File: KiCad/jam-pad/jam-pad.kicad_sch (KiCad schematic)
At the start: 63 parts, among them J1 USB_C, J2 PH_01x03_2.54mm, SW1 MX_Hotswap_LED_RGB, SW13 SW_Push, SW14 RotaryEncoder_Switch, SW15 SW_Push, SW2 MX_Hotswap_LED_RGB, SW3 MX_Hotswap_LED_RGB, SW4 MX_Hotswap_LED_RGB, SW5 MX_Hotswap_LED_RGB, SW6 MX_Hotswap_LED_RGB, SW7 MX_Hotswap_LED_RGB, SW8 MX_Hotswap_LED_RGB, SW9 MX_Hotswap_LED_RGB, U1 RP2040, U3 W25Q16JVSNIQ, U4 MIC5319-3.3YD5, Y1 ECS-120-18-33-JGN

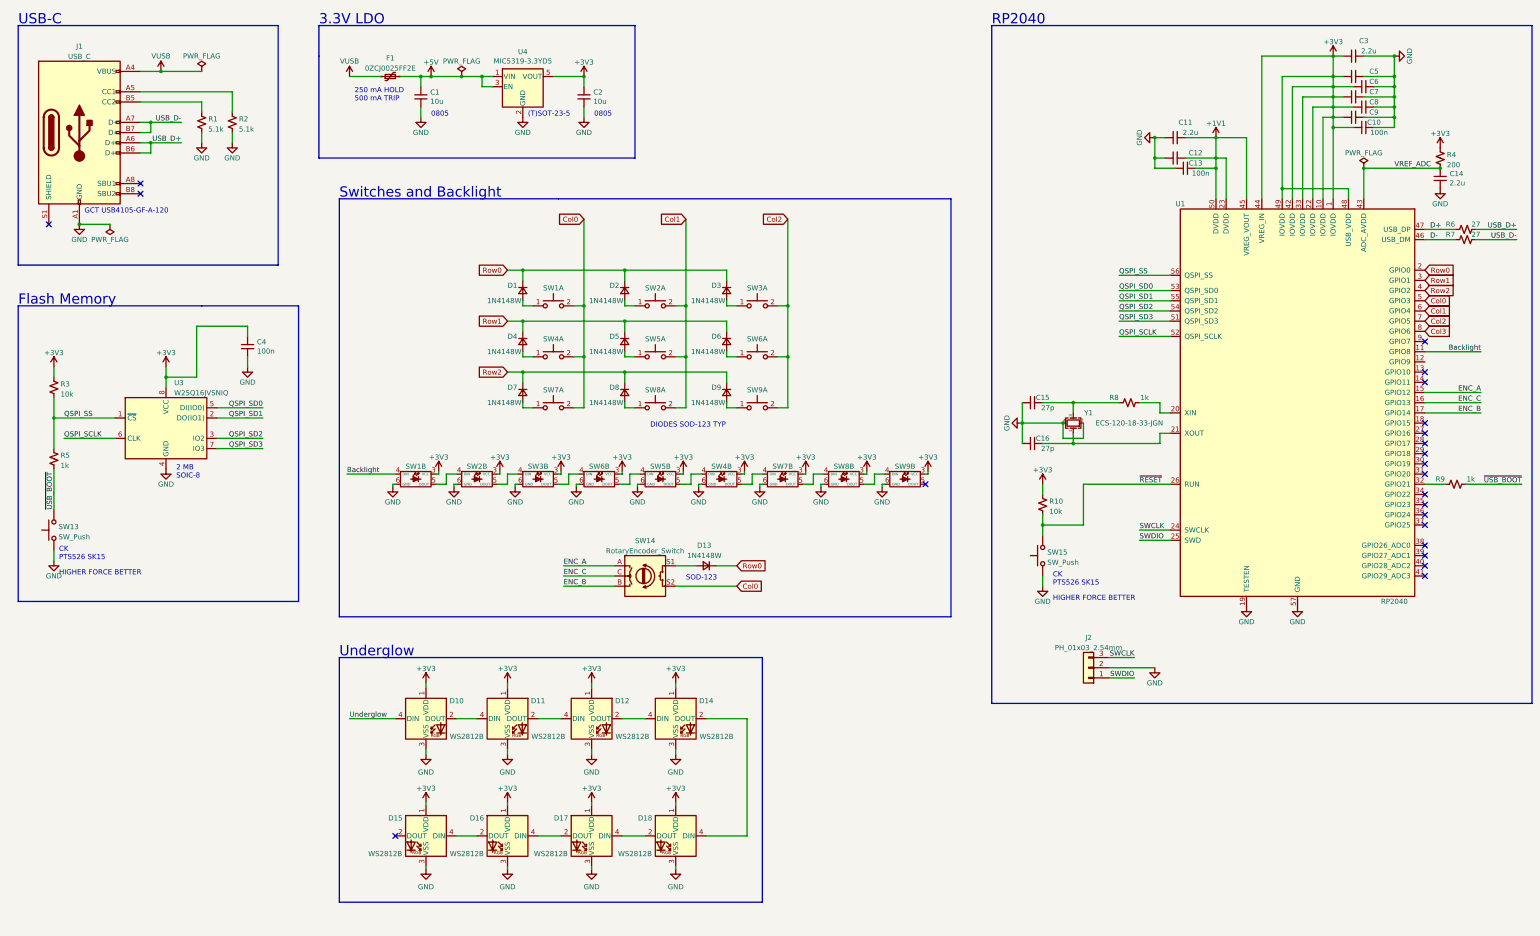
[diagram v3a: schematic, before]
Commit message: changed underglow to knoblight, added led c and r, placed leds
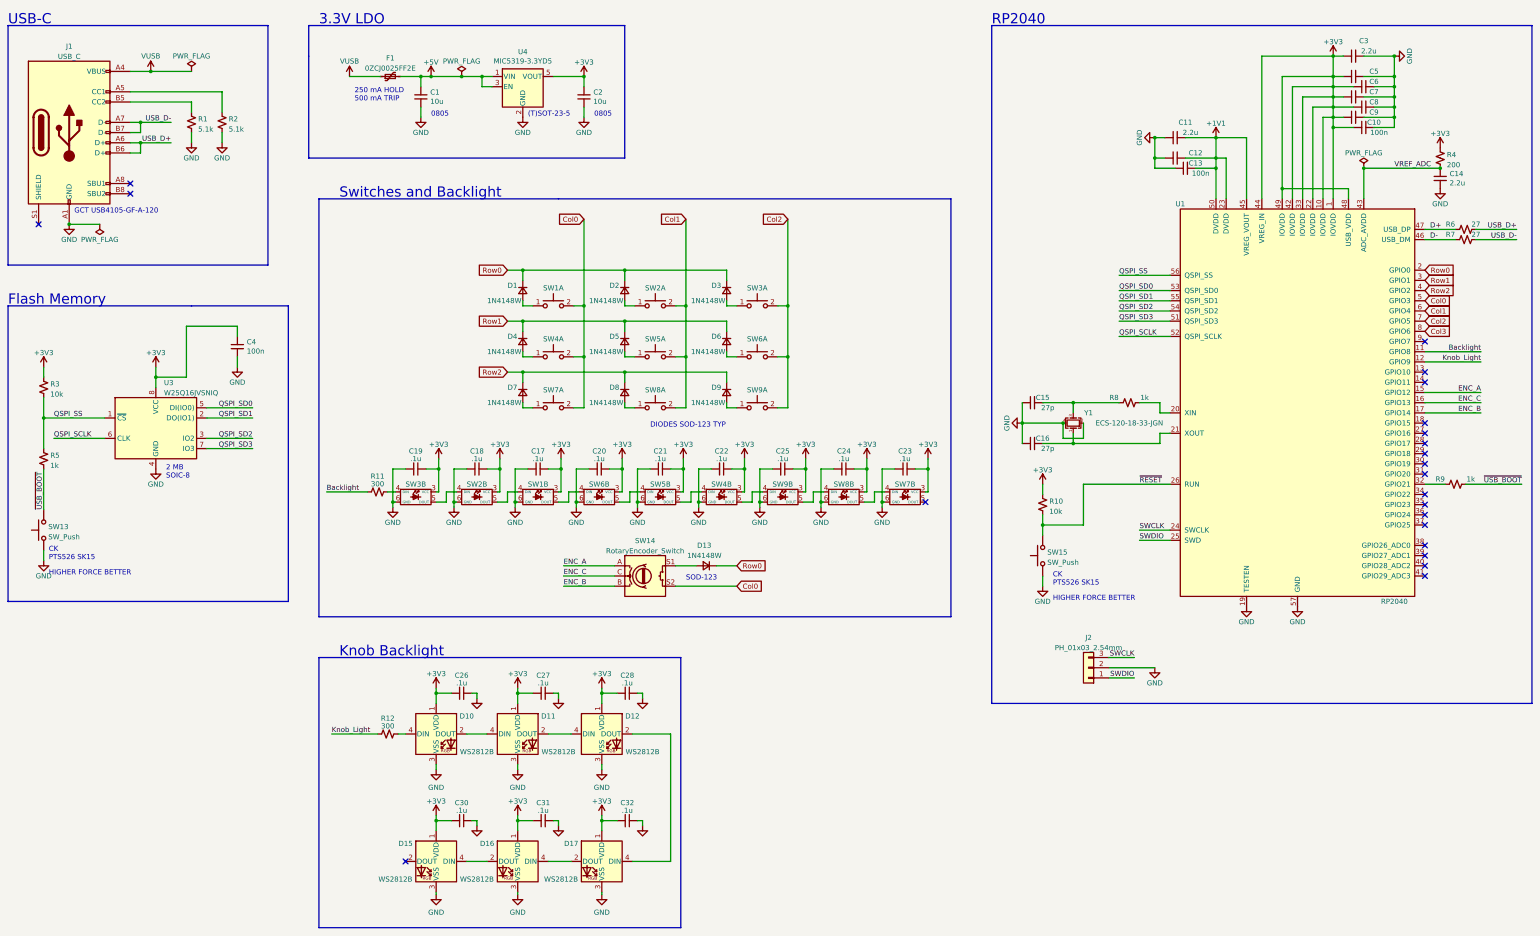
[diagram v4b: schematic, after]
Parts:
- removed D14, D18: WS2812B, LED_SMD:LED_WS2812B_PLCC4_5.0x5.0mm_P3.2mm, symbol LED:WS2812B
- added C17, C18, C19, C20, C21, C22, C23, C24, C25, C26, C27, C28, C30, C31, C32: .1u, Capacitor_SMD:C_0603_1608Metric_Pad1.08x0.95mm_HandSolder, symbol Device:C_Small
- added R11, R12: 300, Resistor_SMD:R_0603_1608Metric_Pad0.98x0.95mm_HandSolder, symbol Device:R_Small_US
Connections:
- net +3V3: now also C17.1, C18.1, C19.1, C20.1, C21.1, C22.1, C23.1, C24.1, C25.1, C26.2, C27.2, C28.2, C30.2, C31.2, C32.2
- net Backlight: now also R11.1; no longer SW1.4 (DIN)
- net GND: now also C17.2, C18.2, C19.2, C20.2, C21.2, C22.2, C23.2, C24.2, C25.2, C26.1, C27.1, C28.1, C30.1, C31.1, C32.1
- net at D17.4 (DIN): now also D12.2 (DOUT)
- net at SW9.4 (DIN): now also SW4.5 (DOUT); no longer SW8.5 (DOUT)
- net at SW9.5 (DOUT): now also SW8.4 (DIN)
- net Knob_Light: now reaches U1.12 (GPIO9)
- net Knob_Light: now also R12.1
- net at SW6.4 (DIN): now also SW1.5 (DOUT); no longer SW3.5 (DOUT)
- net at SW2.4 (DIN): now also SW3.5 (DOUT); no longer SW1.5 (DOUT)
- net at SW3.4 (DIN): now also R11.2; no longer SW2.5 (DOUT)
- net at SW7.5 (DOUT): no longer SW8.4 (DIN)
- net at SW7.4 (DIN): now also SW8.5 (DOUT); no longer SW4.5 (DOUT)
- net Underglow: no longer names the net of D10.4 (DIN)
- net Underglow: now also R12.2
- new net: SW1.4 (DIN), SW2.5 (DOUT)
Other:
- note added: "Knob Backlight"
- note removed: "Underglow"
- moved on the sheet: C4, D10, D11, D12, D15, D16, D17, J1, R1, R2, R3, R5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

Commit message: initial routing
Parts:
- SW1, SW2, SW3, SW7, SW8, SW9: footprint jam-pad:MXOnly-1U-Hotswap-SK6812MINI-E -> jam-pad:MXOnly-1U-Hotswap-SK6812MINI-E_180
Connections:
- net at R11.2: now also SW1.4 (DIN); no longer SW3.4 (DIN)
- net at SW9.4 (DIN): now also SW8.5 (DOUT); no longer SW4.5 (DOUT)
- net at SW9.5 (DOUT): no longer SW8.4 (DIN)
- net at SW6.4 (DIN): now also SW3.5 (DOUT); no longer SW1.5 (DOUT)
- net at SW2.5 (DOUT): now also SW3.4 (DIN); no longer SW1.4 (DIN)
- net at SW2.4 (DIN): now also SW1.5 (DOUT); no longer SW3.5 (DOUT)
- net at SW7.4 (DIN): now also SW4.5 (DOUT); no longer SW8.5 (DOUT)
- net at SW7.5 (DOUT): now also SW8.4 (DIN)
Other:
- moved on the sheet: C17, C19, C23, C25, SW1B, SW3B, SW7B, SW9B

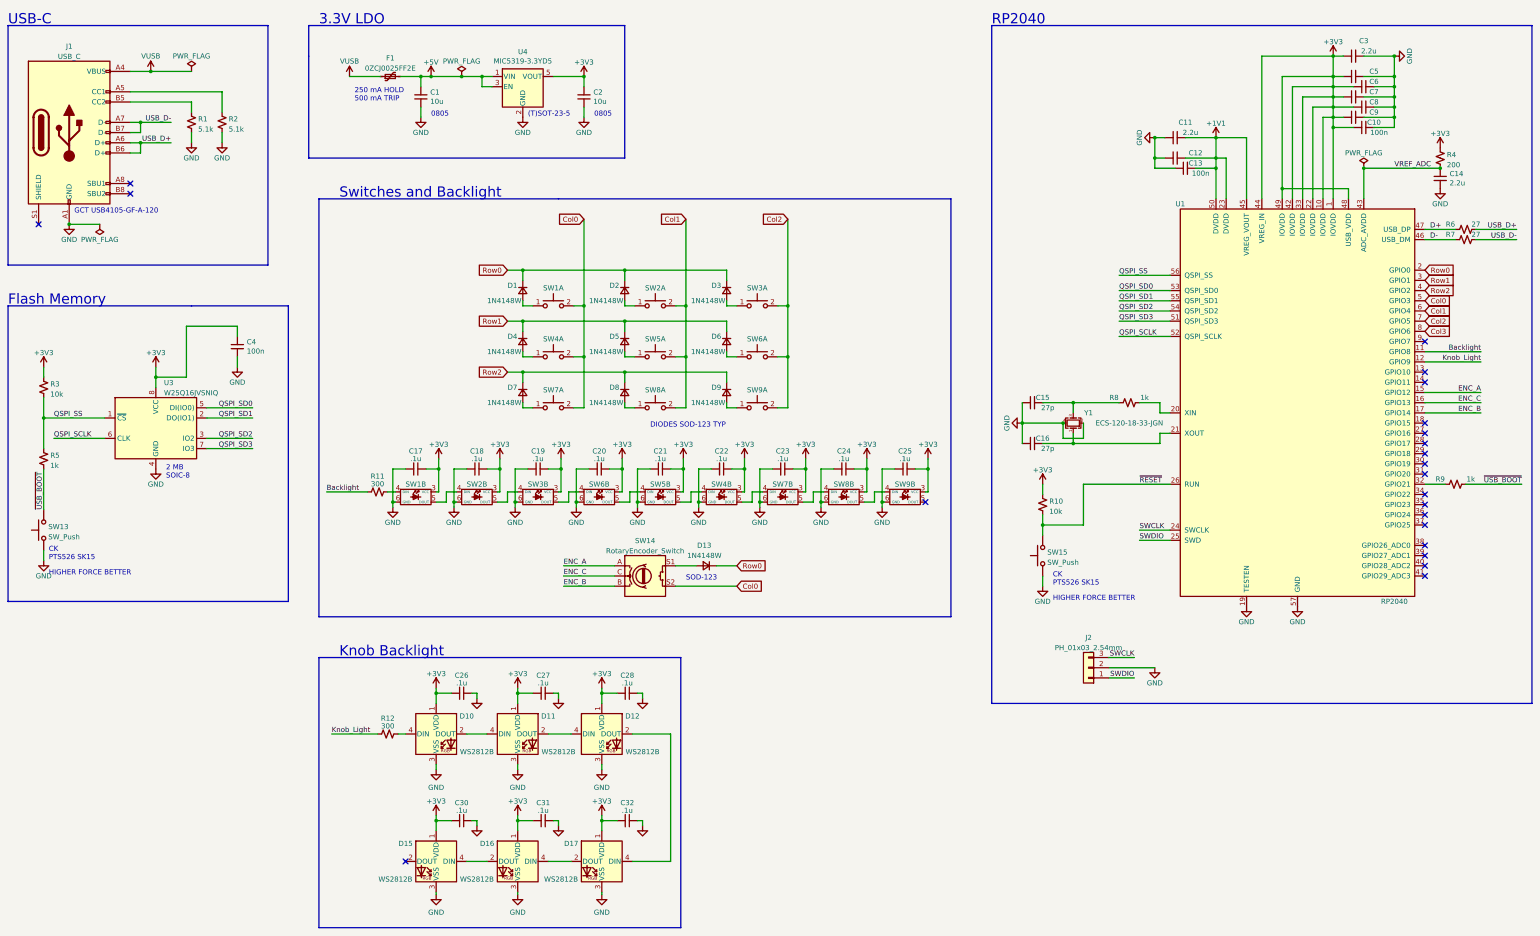
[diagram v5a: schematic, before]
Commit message: mcu placing + routing, power LED on 5V and level shifter
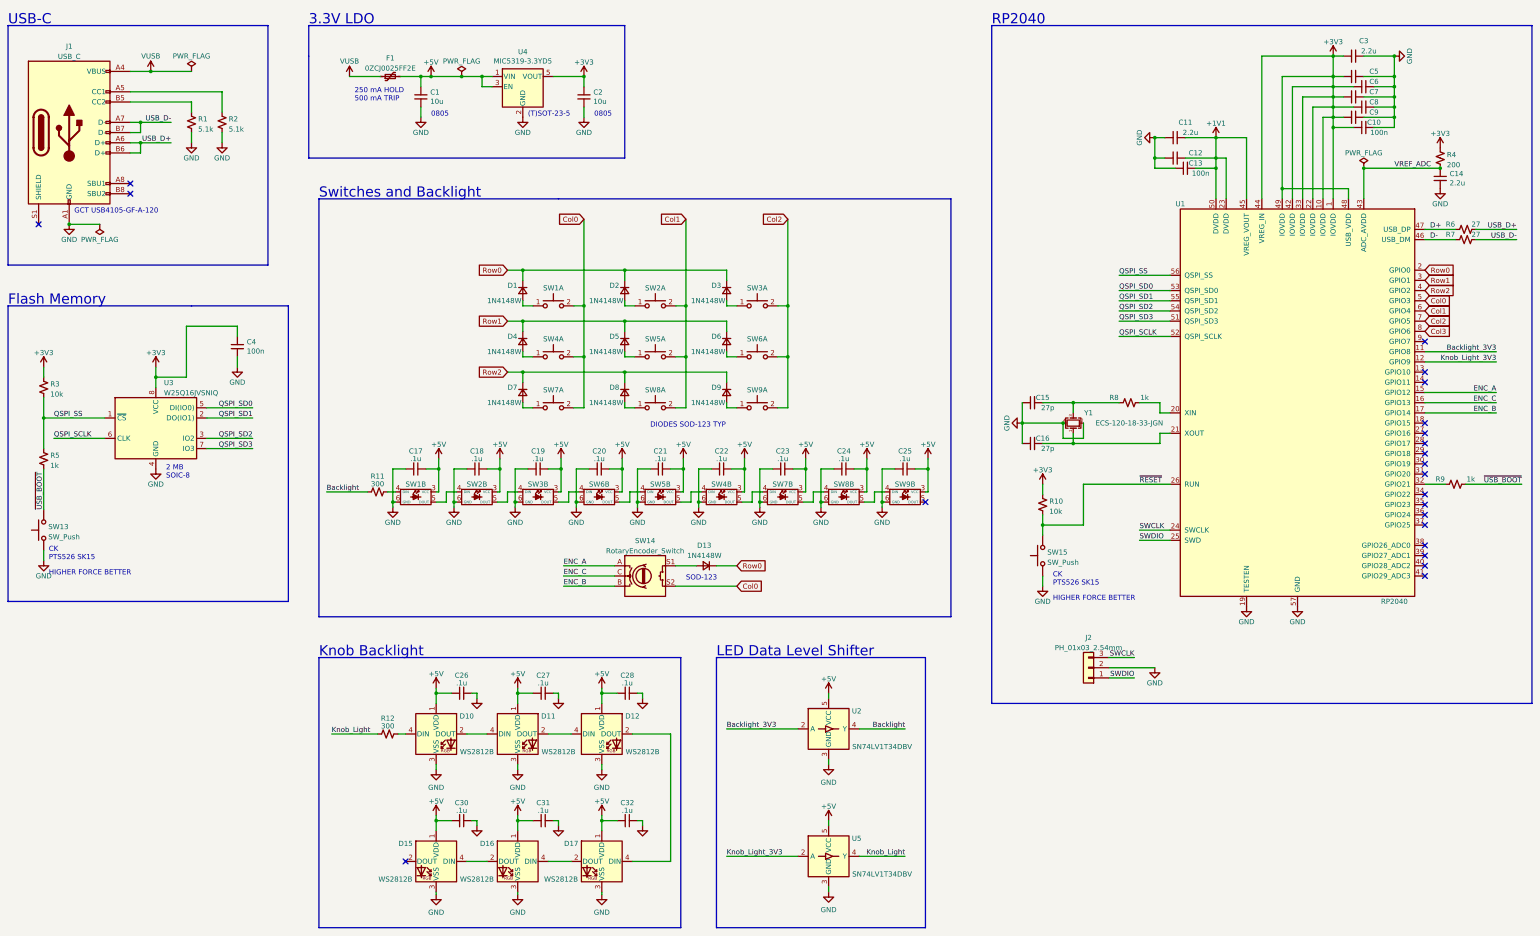
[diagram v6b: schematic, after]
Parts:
- added U2, U5: SN74LV1T34DBV, Package_TO_SOT_SMD:SOT-23-5, symbol Logic_LevelTranslator:SN74LV1T34DBV
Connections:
- net +3V3: no longer C17.1, C18.1, C19.1, C20.1, C21.1, C22.1, C23.1, C24.1, C25.1, C26.2, C27.2, C28.2, C30.2, C31.2, C32.2, D10.1 (VDD), D11.1 (VDD), D12.1 (VDD), D15.1 (VDD), D16.1 (VDD), D17.1 (VDD), SW1.3 (VCC), SW2.3 (VCC), SW3.3 (VCC), SW4.3 (VCC), SW5.3 (VCC), SW6.3 (VCC), SW7.3 (VCC), SW8.3 (VCC), SW9.3 (VCC)
- net +5V: now also C17.1, C18.1, C19.1, C20.1, C21.1, C22.1, C23.1, C24.1, C25.1, C26.2, C27.2, C28.2, C30.2, C31.2, C32.2, D10.1 (VDD), D11.1 (VDD), D12.1 (VDD), D15.1 (VDD), D16.1 (VDD), D17.1 (VDD), SW1.3 (VCC), SW2.3 (VCC), SW3.3 (VCC), SW4.3 (VCC), SW5.3 (VCC), SW6.3 (VCC), SW7.3 (VCC), SW8.3 (VCC), SW9.3 (VCC), U2.5 (VCC), U5.5 (VCC)
- net Backlight: now also U2.4 (Y); no longer U1.11 (GPIO8)
- net GND: now also U2.3 (GND), U5.3 (GND)
- net Knob_Light: now also U5.4 (Y); no longer U1.12 (GPIO9)
- new net Backlight_3V3: U1.11 (GPIO8), U2.2 (A)
- new net Knob_Light_3V3: U1.12 (GPIO9), U5.2 (A)
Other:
- note added: "LED Data Level Shifter"

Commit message: Add symbol fields for KiKit
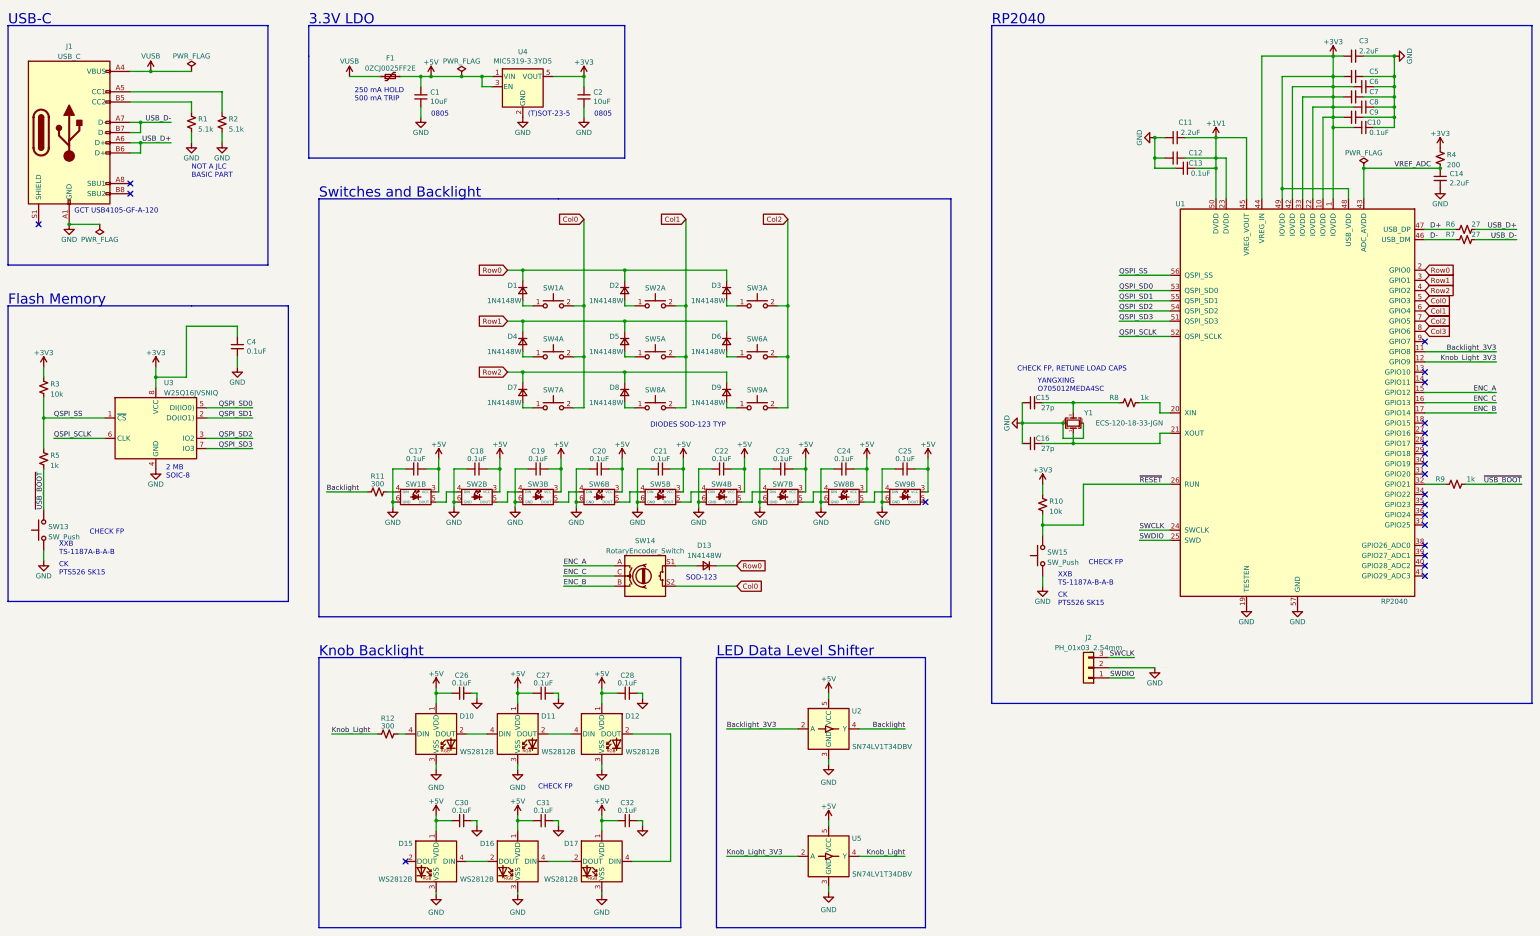
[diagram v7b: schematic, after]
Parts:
- C1, C2: value 10u -> 10uF; LCSC (none) -> C19702
- C10, C12, C13, C4, C5, C6, C7, C8, C9: value 100n -> 0.1uF; LCSC (none) -> C107045
- C11, C14, C3: value 2.2u -> 2.2uF; LCSC (none) -> C23630
- C15, C16: LCSC (none) -> C14663
- C17, C18, C19, C20, C21, C22, C23, C24, C25, C26, C27, C28, C30, C31, C32: value .1u -> 0.1uF; LCSC (none) -> C107045
- D1, D13, D2, D3, D4, D5, D6, D7, D8, D9: LCSC (none) -> C81598
- D10, D11, D12, D15, D16, D17: LCSC (none) -> C2761795
- F1, J1, J2, R1, R2, SW14, U4: JLCPCB_IGNORE (none) -> Y
- R10, R3: LCSC (none) -> C25804
- R11, R12: LCSC (none) -> C23025
- R4: LCSC (none) -> C8218
- R5, R8, R9: LCSC (none) -> C21190
- R6, R7: LCSC (none) -> C25190
- SW13, SW15: LCSC (none) -> C318884
- U1: LCSC (none) -> C2040
- U2, U5: JLCPCB_CORRECTION (none) -> 0; 0; 180; LCSC (none) -> C100024
- U3: LCSC (none) -> C2456211
- Y1: LCSC (none) -> C15918
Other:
- note added: "CHECK FP"
- note added: "CHECK FP, RETUNE LOAD CAPS"
- note added: "NOT A JLC BASIC PART"
- note added: "XXB TS-1187A-B-A-B"
- note added: "YANGXING O705012MEDA4SC"
- note removed: "HIGHER FORCE BETTER"

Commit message: routing adjustments, ec11 standoff, need to fix drc kms
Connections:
- net Col0: no longer SW14.S2
- net Col3: now also SW14.S2
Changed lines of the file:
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@@
     )
   )
-  (global_label "Col0" (shape input) (at 201.93 165.1 0) (fields_autoplaced)
+  (global_label "Col3" (shape input) (at 201.93 165.1 0) (fields_autoplaced)
     (effects (font (size 1.27 1.27)) (justify left))
-    (property "Intersheetrefs" "${INTERSHEET_REFS}" (at 208.6369 165.0206 0)
+    (property "Intersheetrefs" "${INTERSHEET_REFS}" (at 209.1295 165.1 0)
       (effects (font (size 1.27 1.27)) (justify left) hide)
     )
